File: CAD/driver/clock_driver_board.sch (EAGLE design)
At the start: 21 parts, among them U1 MIC5891, U2 MIC5891, U3 HEX_CONVERTERDIP16

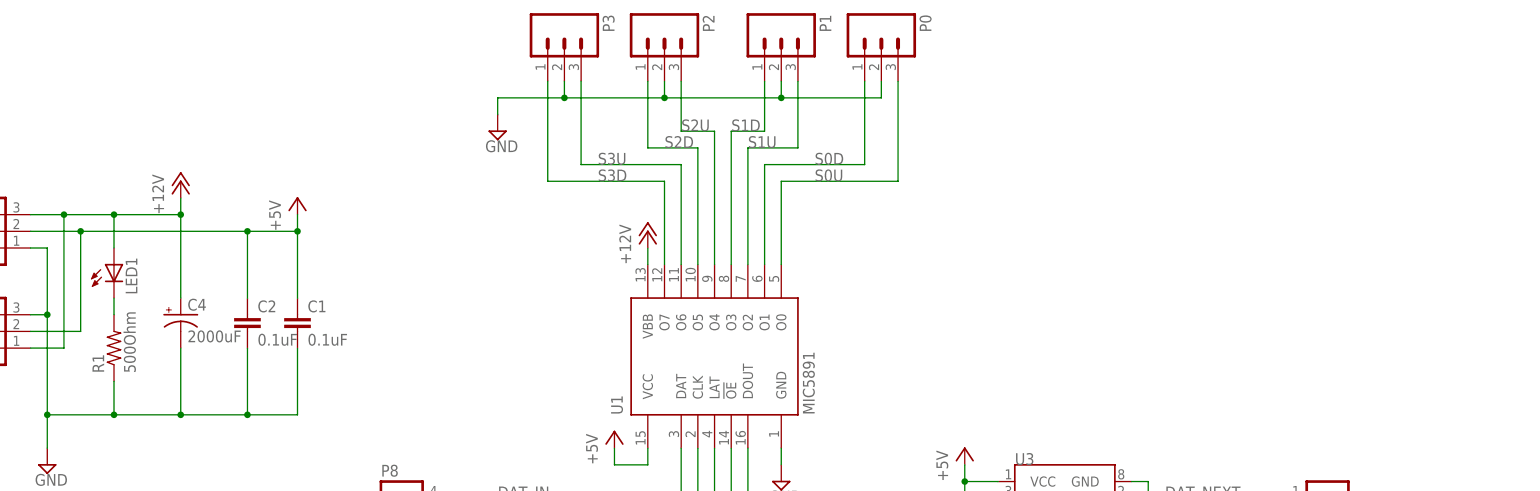
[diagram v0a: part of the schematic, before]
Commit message: Updated driver board CAD files for BOM
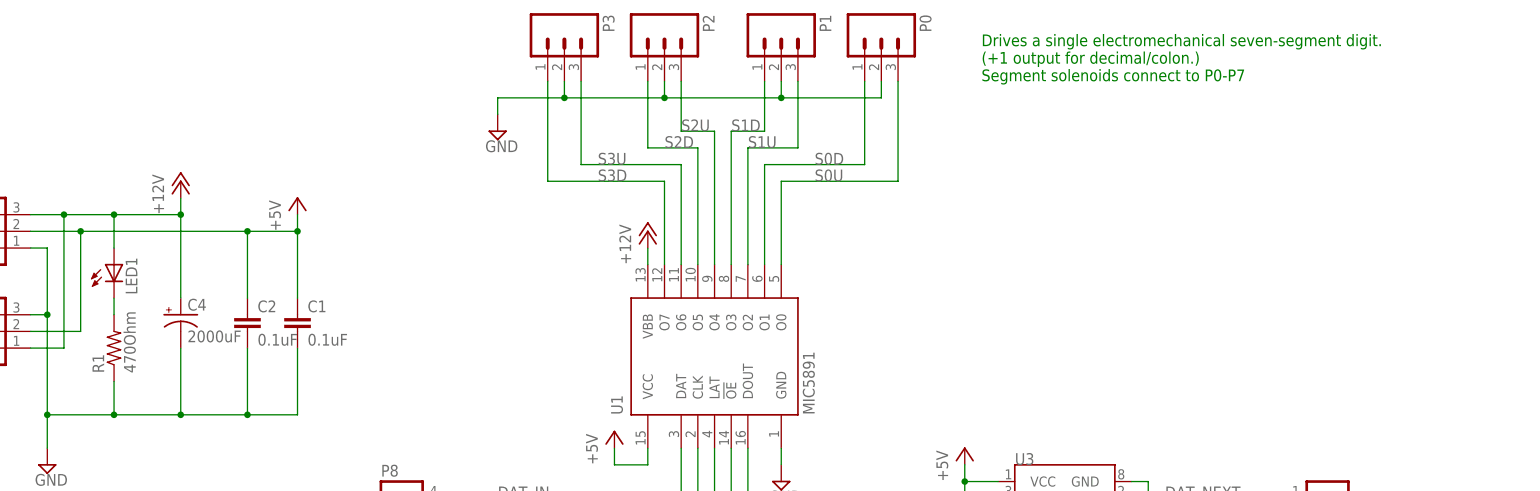
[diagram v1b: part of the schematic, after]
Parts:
- C1, C2, C3: PARTNO (none) -> 21RZ310-RC
- C4: PARTNO (none) -> EEU-TP1E202S
- LED1: PARTNO (none) -> WP7113SRD/D
- P0, P1, P2, P3, P4, P5, P6, P7: BOM (none) -> EXCLUDE
- P10, P11: PARTNO (none) -> 1546551-3
- P8, P9: PARTNO (none) -> 826631-4
- R1: value 500Ohm -> 470Ohm; PARTNO (none) -> CFR-25JR-52-470R
- U1, U2: PARTNO (none) -> MIC5891YN
- U3: PARTNO (none) -> CD74HC4050E
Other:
- note added: "Drives a single electromechanical seven-segment digit. (+1 output for decimal/colon.) Segment solenoids connect to P0-P7"
